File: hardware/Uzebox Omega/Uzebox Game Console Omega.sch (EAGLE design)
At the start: 81 parts, among them CON1 USBSERIALSMD, IC1 MCP1700, IC2 7805T, U5 DC IN, U6 23LC1024, X1 A/V

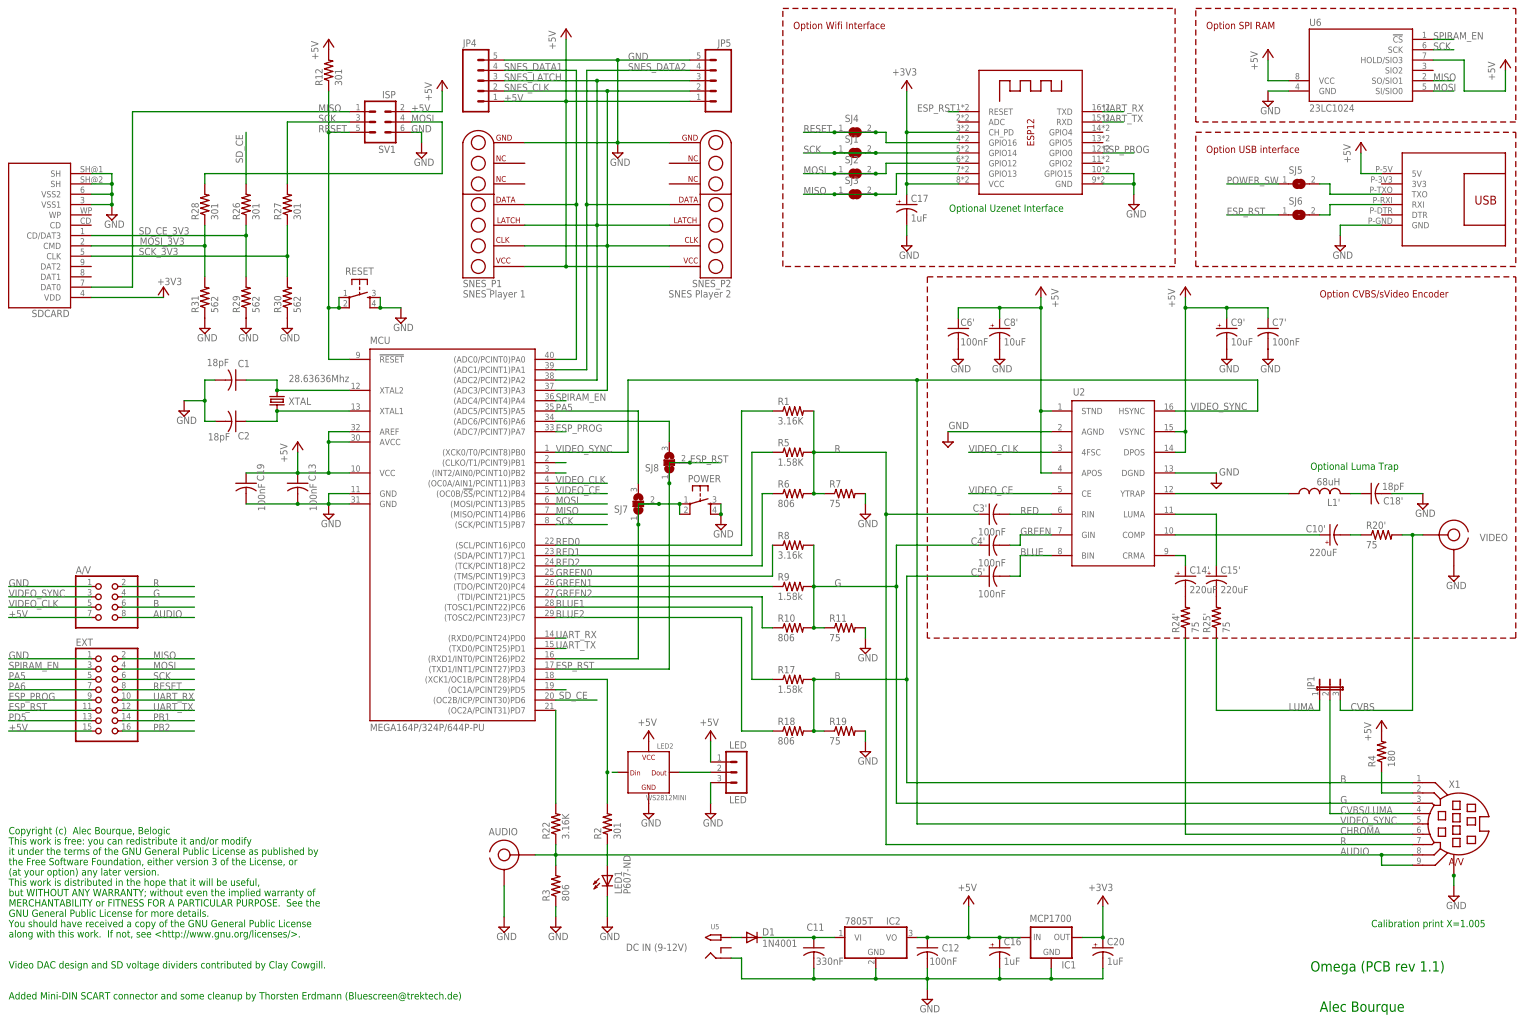
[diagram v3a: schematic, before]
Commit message: Changed RCA sockets and disconnect ISP from ESP by default
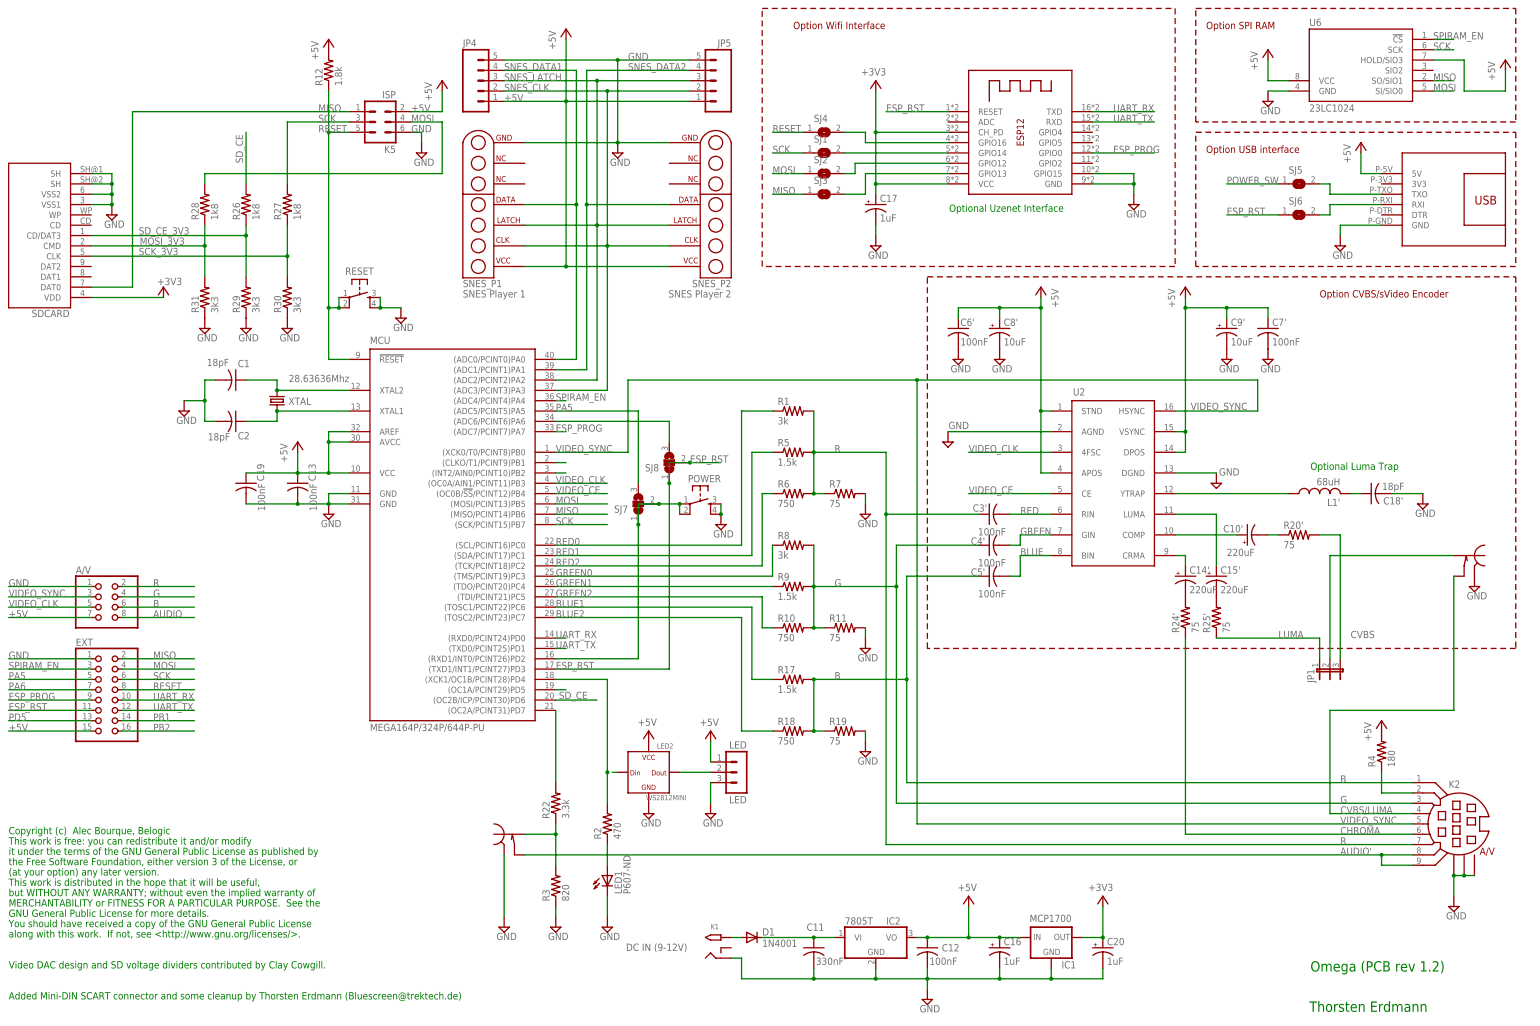
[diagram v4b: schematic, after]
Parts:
- removed AUDIO, VIDEO: RCA, rca:RCA
- added K6, K7: RCA-SWMULTICOMP, Thorsten_connectors:RCA-SWMULTICOMP
- R1: value 3.16K -> 3k
- R10, R18, R6: value 806 -> 750
- R12: value 301 -> 1.8k
- R17, R9: value 1.58k -> 1.5k
- R2: value 301 -> 470
- R22: value 3.16K -> 3.3k
- R26, R27, R28: value 301 -> 1k8
- R29, R30, R31: value 562 -> 3k3
- R3: value 806 -> 820
- R5: value 1.58K -> 1.5k
- R8: value 3.16k -> 3k
- renumbered SV1 to K5, U5 to K1, X1 to K2
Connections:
- new net AUDIO': K2.8, K2.9, K7.SWITCH
- new net N$17: ESP-12.GPIO14, SJ1.2
- new net N$18: ESP-12.GPIO12, SJ2.2
- new net N$19: ESP-12.GPIO13, SJ3.2
- new net N$22: JP1.2, K6.SIGNAL
- new net N$8: ESP-12.GPIO16, SJ4.2
- net AUDIO: now also K7.SIGNAL; no longer AUDIO.SIG, K2.8, K2.9
- net CVBS: no longer VIDEO.SIG
- net CVBS/LUMA: now also K6.SWITCH; no longer JP1.2
- net GND: now also K6.GND, K7.GND; no longer AUDIO.GND, VIDEO.GND
- net MISO: no longer ESP-12.GPIO13, SJ3.2
- net MOSI: no longer ESP-12.GPIO12, SJ2.2
- net RESET: no longer ESP-12.GPIO16, SJ4.2
- net SCK: no longer ESP-12.GPIO14, SJ1.2
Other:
- note added: "Omega (PCB rev 1.2)"
- note added: "Thorsten Erdmann"
- note removed: "Alec Bourque"
- note removed: "Calibration print X=1.005"
- note removed: "Omega (PCB rev 1.1)"
- moved on the sheet: C17, JP1, R20', R22, SJ1, SJ2, SJ3, SJ4

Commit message: Added optional uSD slot
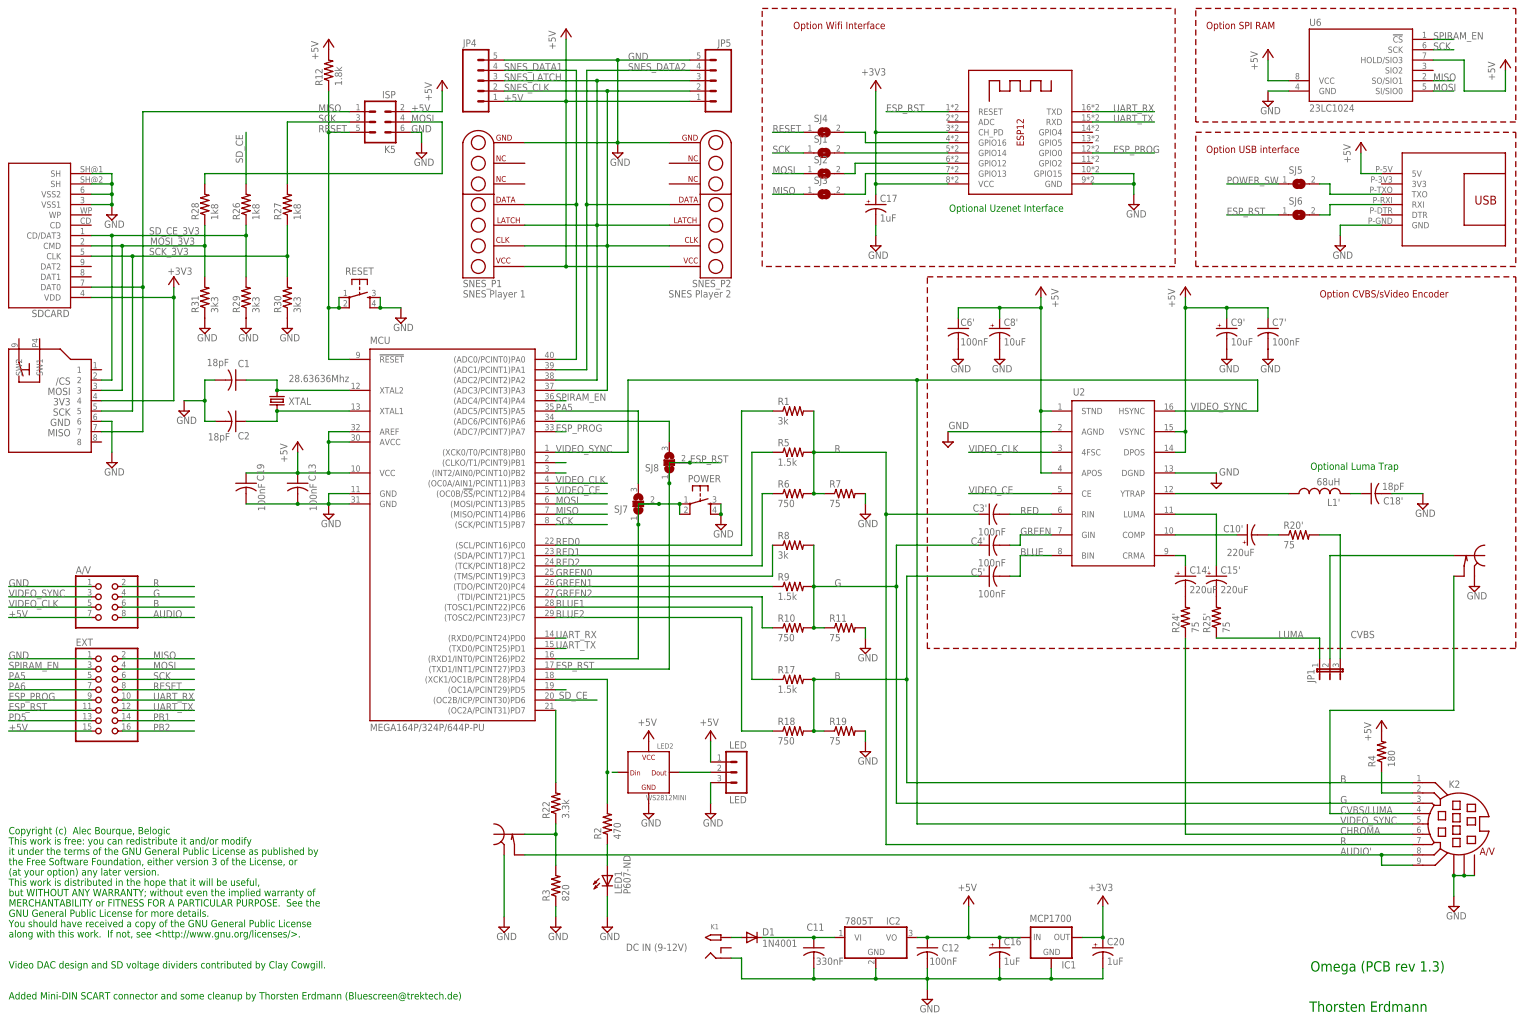
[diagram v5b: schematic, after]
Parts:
- added J1: MICROSD-SWITCH, Thorsten_diverses:MICROSD-SWITCH
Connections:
- net +3V3: now also J1.4
- net GND: now also J1.6
- net MISO: now also J1.7
- net MOSI_3V3: now also J1.3
- net SCK_3V3: now also J1.5
- net SD_CE_3V3: now also J1.2
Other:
- note added: "Omega (PCB rev 1.3)"
- note removed: "Omega (PCB rev 1.2)"
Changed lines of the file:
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@@
 <part name="SUPPLY13" library="supply2" deviceset="GND" device=""/>
 <part name="SUPPLY21" library="supply2" deviceset="GND" device=""/>
+<part name="J1" library="Thorsten_diverses" deviceset="MICROSD-SWITCH" device=""/>
+<part name="SUPPLY23" library="supply2" deviceset="GND" device=""/>
 </parts>
 <sheets>
@@
 <text x="-66.04" y="-33.02" size="1.778" layer="91">along with this work.  If not, see &lt;http://www.gnu.org/licenses/&gt;.</text>
 <text x="-66.04" y="-40.64" size="1.778" layer="91">Video DAC design and SD voltage dividers contributed by Clay Cowgill.</text>
-<text x="254.254" y="-41.402" size="2.54" layer="91">Omega (PCB rev 1.2)</text>
+<text x="254.254" y="-41.402" size="2.54" layer="91">Omega (PCB rev 1.3)</text>
 <text x="165.354" y="145.542" size="1.778" layer="91">Optional Uzenet Interface</text>
 <text x="-66.04" y="-48.26" size="1.778" layer="91">Added Mini-DIN SCART connector and some cleanup by Thorsten Erdmann (Bluescreen@trektech.de)</text>
@@
 <attribute name="VALUE" x="-42.545" y="141.605" size="1.778" layer="96"/>
 </instance>
-<instance part="+3V3" gate="G$1" x="-27.94" y="127" smashed="yes">
-<attribute name="VALUE" x="-23.368" y="129.286" size="1.778" layer="96" rot="R180"/>
+<instance part="+3V3" gate="G$1" x="-25.4" y="129.54" smashed="yes">
+<attribute name="VALUE" x="-20.828" y="131.826" size="1.778" layer="96" rot="R180"/>
 </instance>
 <instance part="ESP-12" gate="G$1" x="182.88" y="165.1" smashed="yes"/>
@@
 <instance part="SUPPLY21" gate="GND" x="289.56" y="-25.4" smashed="yes">
 <attribute name="VALUE" x="287.655" y="-28.575" size="1.778" layer="96"/>
+</instance>
+<instance part="J1" gate="G$1" x="-55.88" y="99.06" rot="R270"/>
+<instance part="SUPPLY23" gate="GND" x="-40.64" y="83.82" smashed="yes">
+<attribute name="VALUE" x="-42.545" y="80.645" size="1.778" layer="96"/>
 </instance>
 </instances>
@@
 <junction x="292.1" y="-17.78"/>
 </segment>
+<segment>
+<pinref part="J1" gate="G$1" pin="6"/>
+<pinref part="SUPPLY23" gate="GND" pin="GND"/>
+<wire x1="-43.18" y1="93.98" x2="-40.64" y2="93.98" width="0.1524" layer="91"/>
+<wire x1="-40.64" y1="93.98" x2="-40.64" y2="86.36" width="0.1524" layer="91"/>
+</segment>
 </net>
 <net name="G" class="0">
@@
 </segment>
 <segment>
-<wire x1="-35.56" y1="170.18" x2="17.78" y2="170.18" width="0.1524" layer="91"/>
+<wire x1="-33.02" y1="170.18" x2="17.78" y2="170.18" width="0.1524" layer="91"/>
 <pinref part="SDCARD" gate="G$1" pin="DAT0"/>
-<wire x1="-45.72" y1="127" x2="-35.56" y2="127" width="0.1524" layer="91"/>
-<wire x1="-35.56" y1="127" x2="-35.56" y2="170.18" width="0.1524" layer="91"/>
+<wire x1="-45.72" y1="127" x2="-33.02" y2="127" width="0.1524" layer="91"/>
+<wire x1="-33.02" y1="127" x2="-33.02" y2="170.18" width="0.1524" layer="91"/>
 <label x="10.16" y="170.18" size="1.778" layer="95"/>
 <pinref part="K5" gate="1" pin="1"/>
+<pinref part="J1" gate="G$1" pin="7"/>
+<wire x1="-43.18" y1="91.44" x2="-33.02" y2="91.44" width="0.1524" layer="91"/>
+<wire x1="-33.02" y1="91.44" x2="-33.02" y2="127" width="0.1524" layer="91"/>
+<junction x="-33.02" y="127"/>
 </segment>
 <segment>
@@
 <pinref part="SDCARD" gate="G$1" pin="VDD"/>
 <pinref part="+3V3" gate="G$1" pin="+3V3"/>
-<wire x1="-45.72" y1="124.46" x2="-27.94" y2="124.46" width="0.1524" layer="91"/>
+<wire x1="-45.72" y1="124.46" x2="-25.4" y2="124.46" width="0.1524" layer="91"/>
+<pinref part="J1" gate="G$1" pin="4"/>
+<wire x1="-25.4" y1="124.46" x2="-25.4" y2="127" width="0.1524" layer="91"/>
+<wire x1="-43.18" y1="99.06" x2="-25.4" y2="99.06" width="0.1524" layer="91"/>
+<wire x1="-25.4" y1="99.06" x2="-25.4" y2="124.46" width="0.1524" layer="91"/>
+<junction x="-25.4" y="124.46"/>
 </segment>
 <segment>
@@
 <wire x1="-17.78" y1="142.24" x2="-17.78" y2="137.16" width="0.1524" layer="91"/>
 <wire x1="-17.78" y1="137.16" x2="-17.78" y2="129.54" width="0.1524" layer="91"/>
-<wire x1="-17.78" y1="137.16" x2="-45.72" y2="137.16" width="0.1524" layer="91"/>
+<wire x1="-17.78" y1="137.16" x2="-38.1" y2="137.16" width="0.1524" layer="91"/>
 <junction x="-17.78" y="137.16"/>
-<label x="-33.782" y="137.414" size="1.778" layer="95"/>
+<label x="-31.242" y="137.414" size="1.778" layer="95"/>
 <pinref part="R28" gate="G$1" pin="1"/>
 <pinref part="R31" gate="G$1" pin="2"/>
 <pinref part="SDCARD" gate="G$1" pin="CMD"/>
+<pinref part="J1" gate="G$1" pin="3"/>
+<wire x1="-38.1" y1="137.16" x2="-45.72" y2="137.16" width="0.1524" layer="91"/>
+<wire x1="-43.18" y1="101.6" x2="-38.1" y2="101.6" width="0.1524" layer="91"/>
+<wire x1="-38.1" y1="101.6" x2="-38.1" y2="137.16" width="0.1524" layer="91"/>
+<junction x="-38.1" y="137.16"/>
 </segment>
 </net>
@@
 <wire x1="2.54" y1="129.54" x2="2.54" y2="134.62" width="0.1524" layer="91"/>
 <wire x1="2.54" y1="134.62" x2="2.54" y2="142.24" width="0.1524" layer="91"/>
-<wire x1="2.54" y1="134.62" x2="-45.72" y2="134.62" width="0.1524" layer="91"/>
+<wire x1="2.54" y1="134.62" x2="-35.56" y2="134.62" width="0.1524" layer="91"/>
 <junction x="2.54" y="134.62"/>
-<label x="-34.036" y="134.874" size="1.778" layer="95"/>
+<label x="-31.496" y="134.874" size="1.778" layer="95"/>
 <pinref part="R30" gate="G$1" pin="2"/>
 <pinref part="R27" gate="G$1" pin="1"/>
 <pinref part="SDCARD" gate="G$1" pin="CLK"/>
+<pinref part="J1" gate="G$1" pin="5"/>
+<wire x1="-35.56" y1="134.62" x2="-45.72" y2="134.62" width="0.1524" layer="91"/>
+<wire x1="-43.18" y1="96.52" x2="-35.56" y2="96.52" width="0.1524" layer="91"/>
+<wire x1="-35.56" y1="96.52" x2="-35.56" y2="134.62" width="0.1524" layer="91"/>
+<junction x="-35.56" y="134.62"/>
 </segment>
 </net>
@@
 <segment>
 <wire x1="-7.62" y1="129.54" x2="-7.62" y2="139.7" width="0.1524" layer="91"/>
-<label x="-34.036" y="139.954" size="1.778" layer="95"/>
+<label x="-31.496" y="139.954" size="1.778" layer="95"/>
 <pinref part="R29" gate="G$1" pin="2"/>
 <pinref part="R26" gate="G$1" pin="1"/>
 <pinref part="SDCARD" gate="G$1" pin="CD/DAT3"/>
 <wire x1="-7.62" y1="139.7" x2="-7.62" y2="142.24" width="0.1524" layer="91"/>
-<wire x1="-45.72" y1="139.7" x2="-7.62" y2="139.7" width="0.1524" layer="91"/>
+<wire x1="-45.72" y1="139.7" x2="-40.64" y2="139.7" width="0.1524" layer="91"/>
 <junction x="-7.62" y="139.7"/>
-</segment>
-</net>
+<pinref part="J1" gate="G$1" pin="2"/>
+<wire x1="-40.64" y1="139.7" x2="-7.62" y2="139.7" width="0.1524" layer="91"/>
+<wire x1="-43.18" y1="104.14" x2="-40.64" y2="104.14" width="0.1524" layer="91"/>
+<wire x1="-40.64" y1="104.14" x2="-40.64" y2="139.7" width="0.1524" layer="91"/>
+<junction x="-40.64" y="139.7"/>
+</segment>
+</net>
